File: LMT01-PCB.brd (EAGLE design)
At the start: 127 x 30.5 mm, 32 parts, among them IC1 PIC18F47Q84, IC2 +12v, IC3 LM393D, IC5 LM393D, IC6 MAX3465CSD

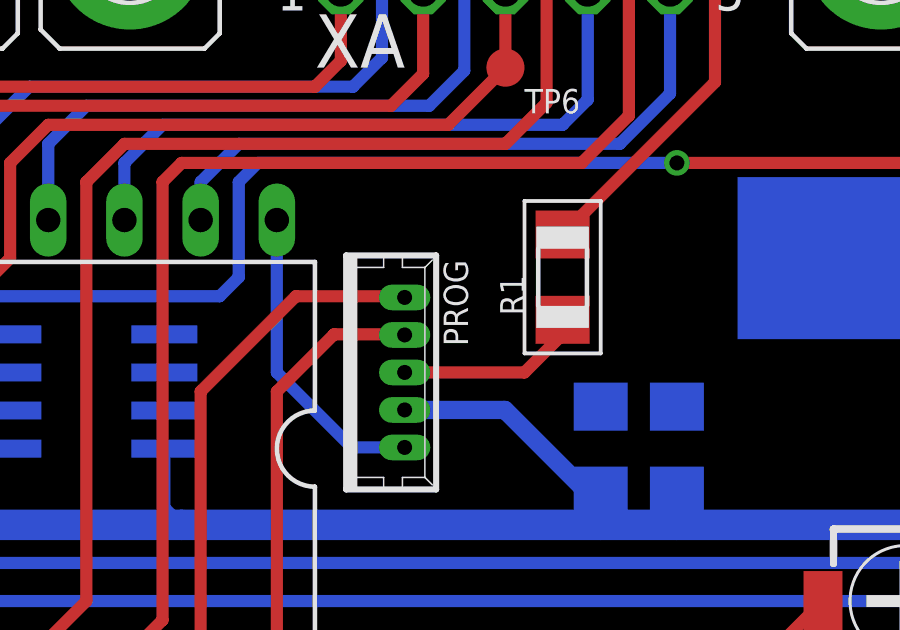
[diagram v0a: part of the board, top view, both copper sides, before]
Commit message: Adding pullup resistor on MCLR
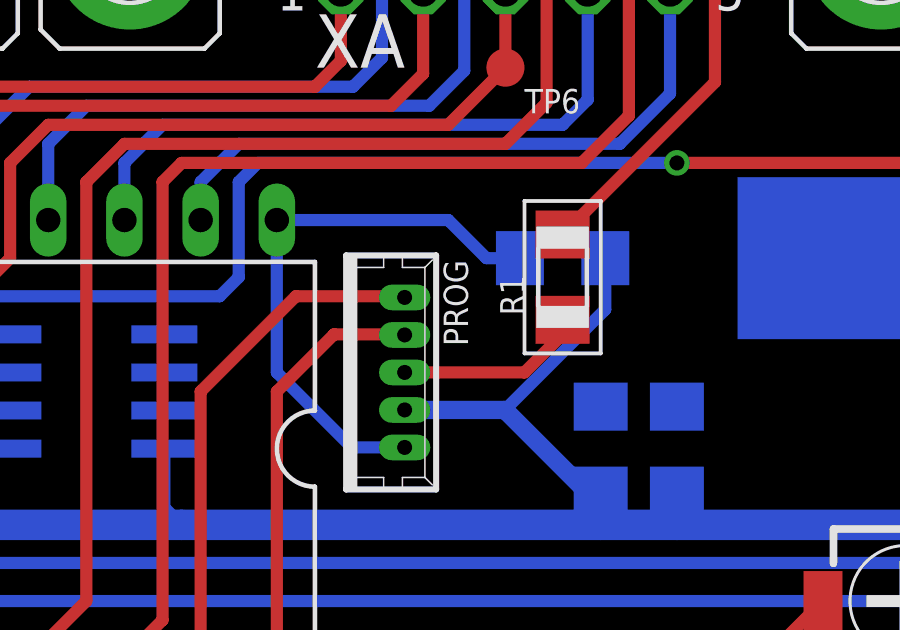
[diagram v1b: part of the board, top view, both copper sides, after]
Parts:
- added R6: 5k, resistor:R1206
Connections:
- net +5V: now also R6.2
- net N$1: now also R6.1
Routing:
- net N$1: track 10.4 -> 19.0 mm
- net +5V: track 152.0 -> 158.5 mm
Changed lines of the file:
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@@
 <attribute name="NAME" x="105.791" y="19.558" size="0.8128" layer="25" font="fixed" ratio="10" rot="R90"/>
+</element>
+<element name="R6" library="resistor" package="R1206" value="5k" x="81.28" y="16.51" smashed="yes" rot="MR180">
+<attribute name="NAME" x="84.455" y="15.875" size="0.8128" layer="26" font="fixed" rot="MR90"/>
 </element>
 </elements>
@@
 <wire x1="105.41" y1="17.78" x2="105.41" y2="13.97" width="0.4064" layer="1"/>
 <wire x1="105.41" y1="13.97" x2="101.6" y2="10.16" width="0.4064" layer="1"/>
+<contactref element="R6" pad="2"/>
+<wire x1="82.702" y1="16.51" x2="82.702" y2="14.797" width="0.4064" layer="16"/>
+<wire x1="82.702" y1="14.797" x2="79.355" y2="11.45" width="0.4064" layer="16"/>
 </signal>
 <signal name="UARTRX">
@@
 <wire x1="74.255" y1="10.2" x2="71.755" y2="12.7" width="0.4064" layer="16"/>
 <wire x1="71.755" y1="12.7" x2="71.755" y2="17.78" width="0.4064" layer="16"/>
+<contactref element="R6" pad="1"/>
+<wire x1="71.755" y1="17.78" x2="77.47" y2="17.78" width="0.4064" layer="16"/>
+<wire x1="77.47" y1="17.78" x2="78.74" y2="16.51" width="0.4064" layer="16"/>
+<wire x1="78.74" y1="16.51" x2="79.858" y2="16.51" width="0.4064" layer="16"/>
 </signal>
 <signal name="N$2">
